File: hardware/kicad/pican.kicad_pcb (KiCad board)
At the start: 2 copper layers, 54.6 x 41.9 mm, 13 parts, among them P1 CONN_01X06, P2 CONN_01X03, U1 MCP2515, U2 MCP2562, Y1 16MHz

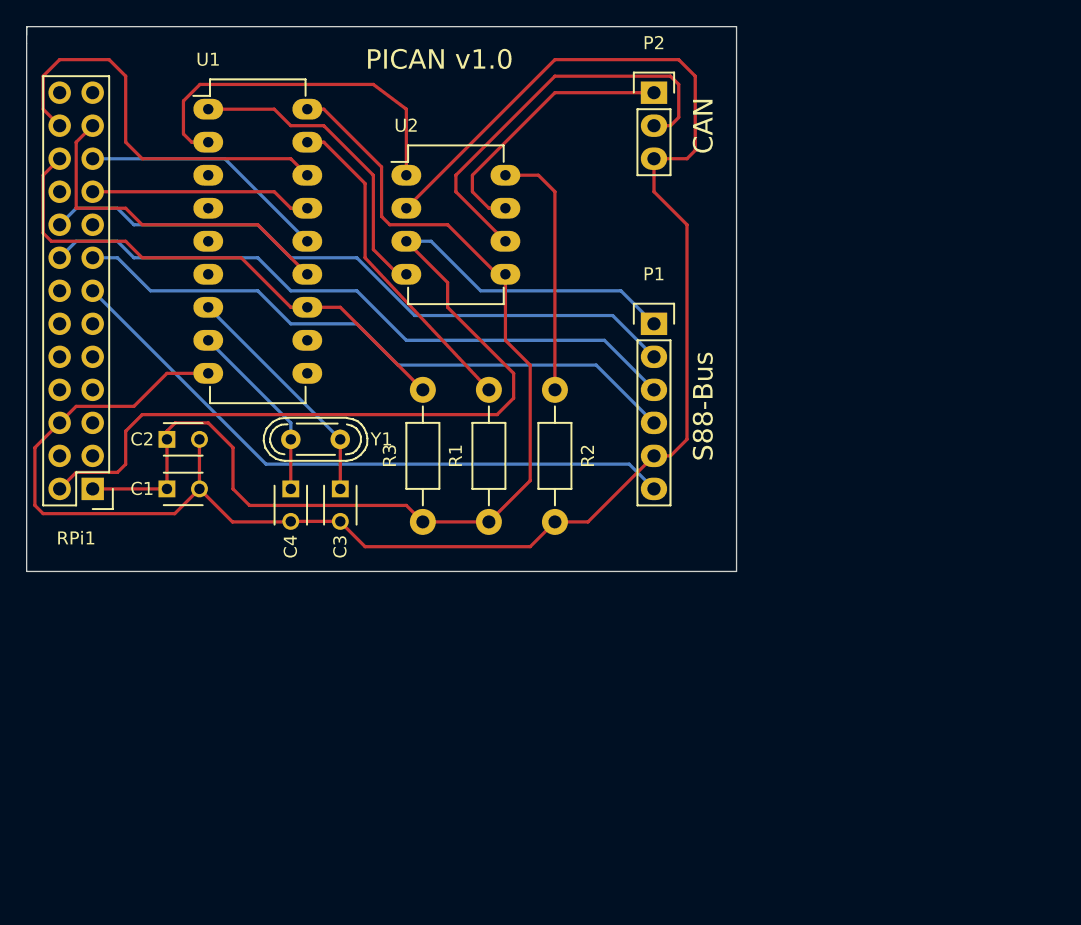
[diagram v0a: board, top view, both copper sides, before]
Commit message: Add optocoupler and started new PCB.
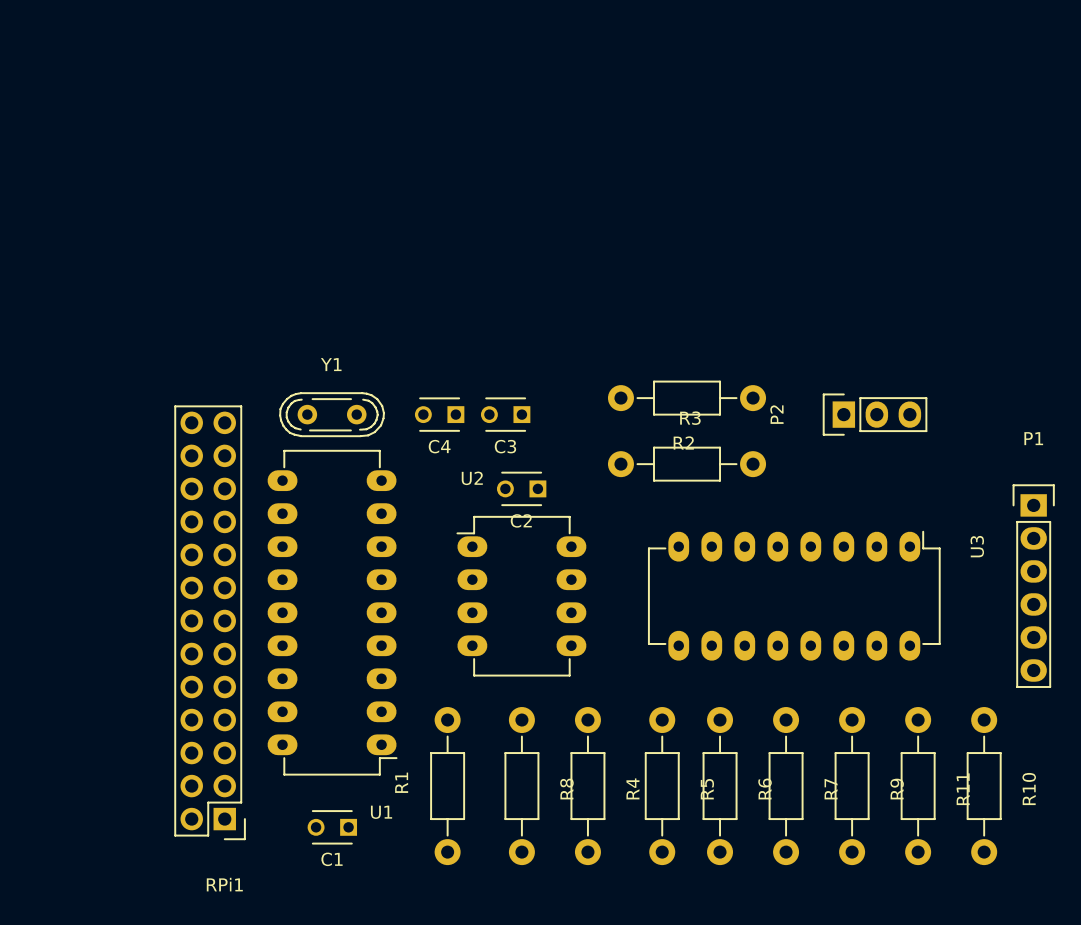
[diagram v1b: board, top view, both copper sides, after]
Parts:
- added R10: 10k, Resistors_ThroughHole:Resistor_Horizontal_RM10mm, F.Cu at (174.0, 118.1)
- added R11: 10k, Resistors_ThroughHole:Resistor_Horizontal_RM10mm, F.Cu at (168.9, 118.1)
- added R4: 270, Resistors_ThroughHole:Resistor_Horizontal_RM10mm, F.Cu at (143.5, 118.1)
- added R5: 270, Resistors_ThroughHole:Resistor_Horizontal_RM10mm, F.Cu at (149.2, 118.1)
- added R6: 270, Resistors_ThroughHole:Resistor_Horizontal_RM10mm, F.Cu at (153.7, 118.1)
- added R7: 390, Resistors_ThroughHole:Resistor_Horizontal_RM10mm, F.Cu at (158.8, 118.1)
- added R8: 10k, Resistors_ThroughHole:Resistor_Horizontal_RM10mm, F.Cu at (138.4, 118.1)
- added R9: 10k, Resistors_ThroughHole:Resistor_Horizontal_RM10mm, F.Cu at (163.8, 118.1)
- added U3: LTV-847, Housings_DIP:DIP-16_W7.62mm_LongPads, F.Cu at (168.3, 99.7)
- moved U1 50.7 mm to (127.6, 114.9), turned to 180 degrees
- moved P1 32.4 mm to (177.8, 96.5)
- moved C1 29.5 mm to (125.1, 121.3), turned to 180 degrees
- moved U2 29.0 mm to (134.6, 99.7)
- moved C2 28.8 mm to (139.7, 95.2), turned to 180 degrees
- moved P2 28.8 mm to (163.2, 89.5), turned to 90 degrees
- moved RPi1 27.4 mm to (115.6, 120.7)
- moved R1 25.6 mm to (132.7, 118.1)
- moved R3 20.3 mm to (151.1, 93.3), turned to 0 degrees
- moved C3 15.1 mm to (138.4, 89.5), turned to 180 degrees
- moved C4 13.9 mm to (133.3, 89.5), turned to 180 degrees
- moved R2 11.1 mm to (151.1, 88.3), turned to 180 degrees
- moved Y1 2.29 mm to (123.8, 89.5), turned to 0 degrees
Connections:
- P1 pad 1: +5V -> /S88_DATA
- P1 pad 2: /S88_RESET -> GNDD
- P1 pad 3: /S88_PS -> /S88_CLOCK
- P1 pad 4: /S88_CLOCK -> /S88_LOAD
- P1 pad 5: GND -> /S88_RESET
- P1 pad 6: /S88_DATA -> +5VD
- RPi1 pad 10: (no net) -> Net-(RPi1-Pad10)
- RPi1 pad 11: (no net) -> Net-(RPi1-Pad11)
- RPi1 pad 12: (no net) -> Net-(RPi1-Pad12)
- RPi1 pad 13: /S88_DATA -> /GPIO_S88_DATA
- RPi1 pad 14: (no net) -> Net-(RPi1-Pad14)
- RPi1 pad 15: /S88_CLOCK -> /GPIO_S88_CLOCK
- RPi1 pad 16: /S88_PS -> /GPIO_S88_LOAD
- RPi1 pad 17: (no net) -> Net-(RPi1-Pad17)
- RPi1 pad 18: /S88_RESET -> /GPIO_S88_RESET
- RPi1 pad 20: (no net) -> Net-(RPi1-Pad20)
- RPi1 pad 25: (no net) -> Net-(RPi1-Pad25)
- RPi1 pad 26: (no net) -> Net-(RPi1-Pad26)
- RPi1 pad 3: (no net) -> /I2C_SDA
- RPi1 pad 4: (no net) -> Net-(RPi1-Pad4)
- RPi1 pad 5: (no net) -> /I2C_SCL
- RPi1 pad 7: (no net) -> Net-(RPi1-Pad7)
- RPi1 pad 8: (no net) -> Net-(RPi1-Pad8)
- RPi1 pad 9: (no net) -> Net-(RPi1-Pad9)
- U1 pad 10: (no net) -> Net-(U1-Pad10)
- U1 pad 11: (no net) -> Net-(U1-Pad11)
- U1 pad 3: (no net) -> Net-(U1-Pad3)
- U1 pad 4: (no net) -> Net-(U1-Pad4)
- U1 pad 5: (no net) -> Net-(U1-Pad5)
- U1 pad 6: (no net) -> Net-(U1-Pad6)
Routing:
- net GND: track 139.8 -> 0.00 mm
- net +3V3: track 84.1 -> 0.00 mm
- net +5V: track 77.1 -> 0.00 mm
- net /S88_RESET: track 51.0 -> 0.00 mm
- net /S88_PS: track 51.0 -> 0.00 mm
- net /S88_DATA: track 49.5 -> 0.00 mm
- net /S88_CLOCK: track 48.4 -> 0.00 mm
- net Net-(R3-Pad1): track 40.4 -> 0.00 mm
- net Net-(P2-Pad2): track 31.9 -> 0.00 mm
- net /SPI_CS: track 31.8 -> 0.00 mm
- net Net-(U1-Pad2): track 28.1 -> 0.00 mm
- net /SPI_CLK: track 26.8 -> 0.00 mm
- net Net-(R1-Pad2): track 25.4 -> 0.00 mm
- net Net-(U1-Pad1): track 23.8 -> 0.00 mm
- net Net-(P2-Pad1): track 20.9 -> 0.00 mm
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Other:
- board outline removed
- board text removed: "CAN"
- board text removed: "PICAN v1.0"
- board text removed: "S88-Bus"
